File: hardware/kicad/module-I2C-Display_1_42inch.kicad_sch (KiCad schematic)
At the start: 33 parts, among them J1 JST 4 Pin Qwiic I2C Connector, J2 JST 4 Pin Qwiic I2C Connector, J3 noknok_FlashPads_I2C-module, J4 noknok_UART_debug_1x3_pogo, Q1 2N7002, U1 CH32V003F4U6, U2 MT3540‑F23

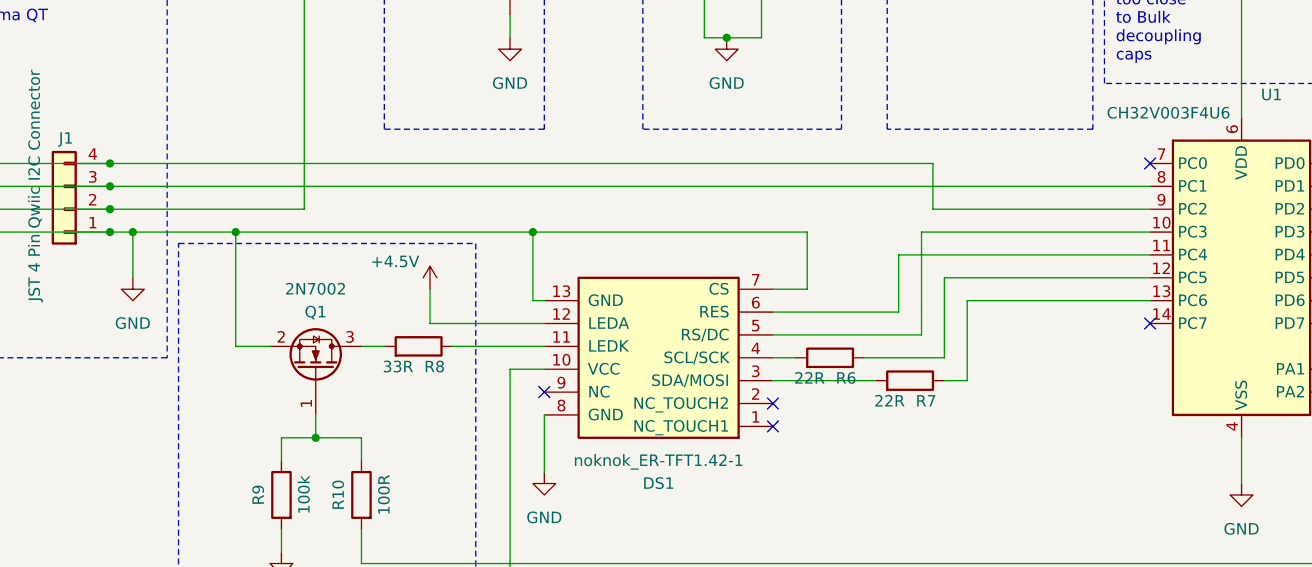
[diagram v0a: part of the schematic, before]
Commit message: hardware: update KiCad layout and schematic, add BOM and schematic PDF
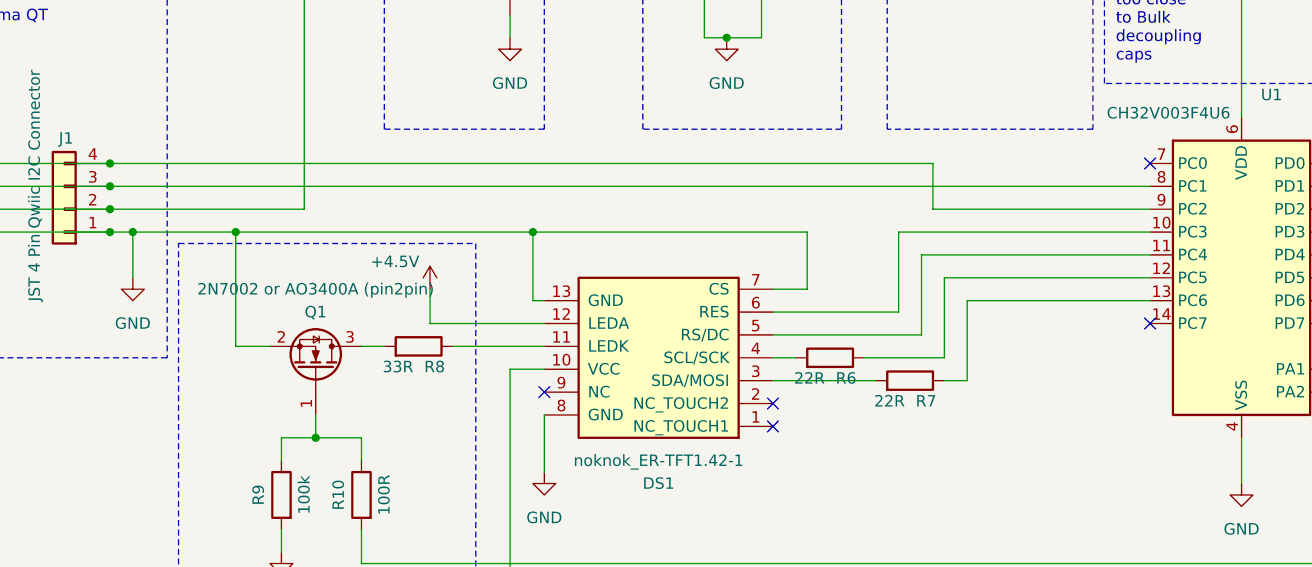
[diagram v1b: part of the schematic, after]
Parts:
- Q1: value 2N7002 -> 2N7002 or AO3400A (pin2pin)
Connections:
- net at DS1.5 (RS/DC): now also U1.11 (PC4); no longer U1.10 (PC3)
- net at DS1.6 (RES): now also U1.10 (PC3); no longer U1.11 (PC4)
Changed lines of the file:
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@@
 	(wire
 		(pts
+			(xy 132.08 107.95) (xy 157.48 107.95)
+		)
+		(stroke
+			(width 0)
+			(type default)
+		)
+	)
+	(wire
+		(pts
 			(xy 234.95 104.14) (xy 224.79 104.14)
 		)
@@
 	(wire
 		(pts
-			(xy 132.08 105.41) (xy 132.08 116.84)
+			(xy 247.65 58.42) (xy 257.81 58.42)
 		)
 		(stroke
@@
 	(wire
 		(pts
-			(xy 247.65 58.42) (xy 257.81 58.42)
+			(xy 157.48 105.41) (xy 129.54 105.41)
 		)
 		(stroke
@@
 	(wire
 		(pts
-			(xy 129.54 107.95) (xy 129.54 114.3)
+			(xy 129.54 105.41) (xy 129.54 114.3)
 		)
 		(stroke
@@
 	(wire
 		(pts
-			(xy 60.96 138.43) (xy 60.96 140.97)
+			(xy 132.08 107.95) (xy 132.08 116.84)
 		)
 		(stroke
@@
 	(wire
 		(pts
-			(xy 41.91 105.41) (xy 44.45 105.41)
+			(xy 60.96 138.43) (xy 60.96 140.97)
 		)
 		(stroke
@@
 	(wire
 		(pts
-			(xy 137.16 121.92) (xy 134.62 121.92)
+			(xy 41.91 105.41) (xy 44.45 105.41)
 		)
 		(stroke
@@
 	(wire
 		(pts
-			(xy 41.91 102.87) (xy 63.5 102.87)
+			(xy 137.16 121.92) (xy 134.62 121.92)
 		)
 		(stroke
@@
 	(wire
 		(pts
-			(xy 157.48 105.41) (xy 132.08 105.41)
+			(xy 41.91 102.87) (xy 63.5 102.87)
 		)
 		(stroke
@@
 	(wire
 		(pts
-			(xy 157.48 107.95) (xy 129.54 107.95)
-		)
-		(stroke
-			(width 0)
-			(type default)
-		)
-	)
-	(wire
-		(pts
 			(xy 27.94 100.33) (xy 41.91 100.33)
 		)
@@
 			)
 		)
-		(property "Value" "2N7002"
+		(property "Value" "2N7002 or AO3400A (pin2pin)"
 			(at 64.77 111.76 90)
 			(show_name no)
